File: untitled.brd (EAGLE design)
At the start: 54.8 x 54.7 mm, 25 parts

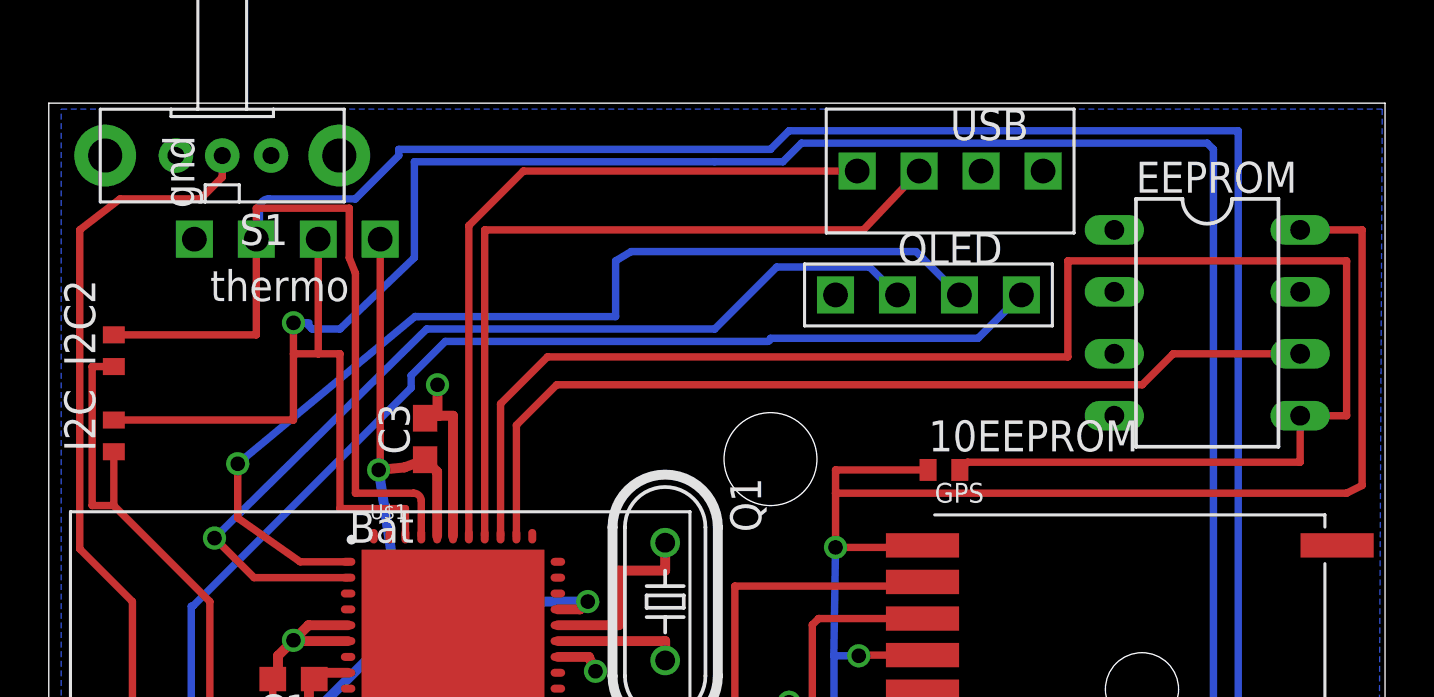
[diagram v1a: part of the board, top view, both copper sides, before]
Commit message: moved eeprom
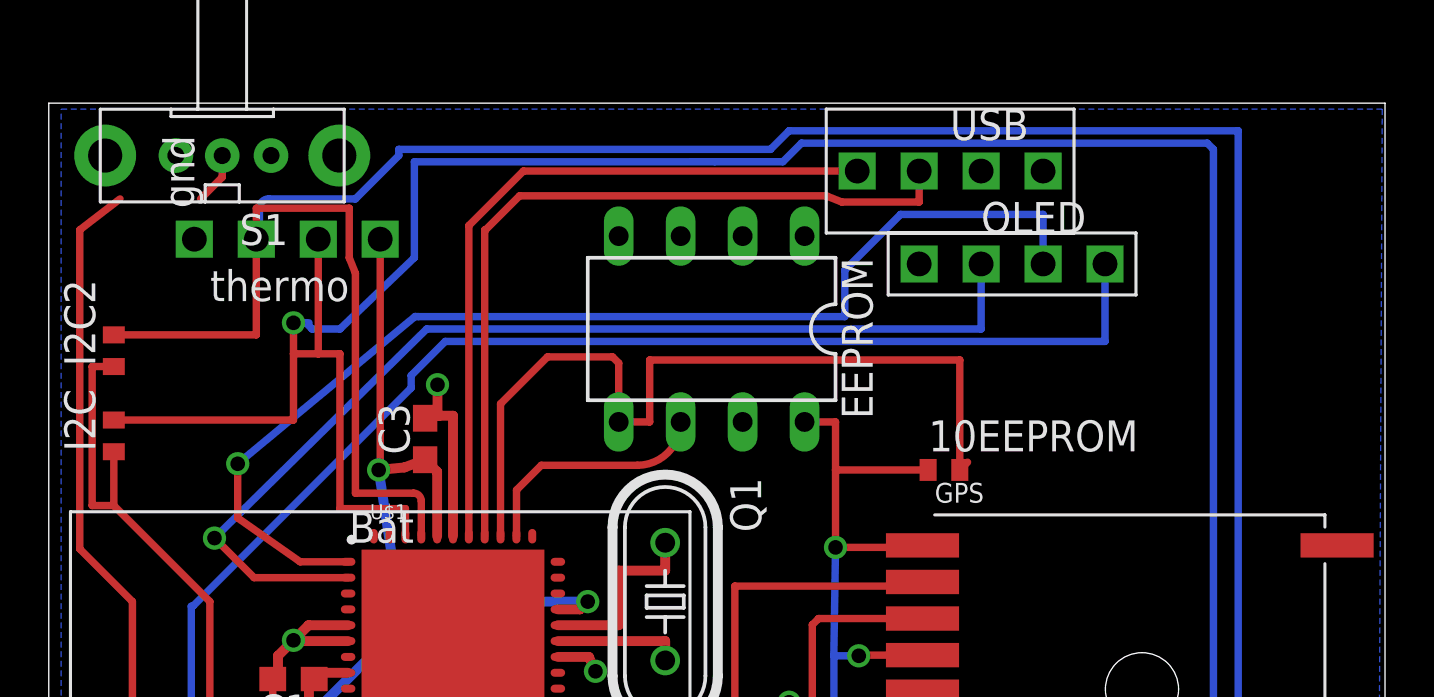
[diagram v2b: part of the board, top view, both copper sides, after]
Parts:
- moved EEPROM 20.3 mm to (65.4, 55.6), turned to 180 degrees
- moved OLED_SCREEN 3.66 mm to (79.0, 58.3)
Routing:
- net N$18: track 69.1 -> 35.1 mm
- net +3V3: track 270.3 -> 238.8 mm
- net N$19: track 37.9 -> 9.78 mm
- net +5V: track 57.5 -> 63.4 mm
- net N$11: track 42.2 -> 47.4 mm
- net N$10: track 39.2 -> 43.8 mm
- net N$13: track 28.9 -> 25.6 mm
- net N$9: track 31.4 -> 32.3 mm
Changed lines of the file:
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@@
 <wire x1="38.227" y1="64.887" x2="38.227" y2="10.16" width="0" layer="20"/>
 <text x="45.72" y="11.7475" size="1.778" layer="1">FG-1136</text>
-<hole x="67.818" y="50.292" drill="3.81"/>
 <rectangle x1="54.5465" y1="28.7655" x2="54.6735" y2="28.8925" layer="22"/>
 <rectangle x1="66.7385" y1="28.7655" x2="66.8655" y2="28.8925" layer="22"/>
@@
 <elements>
 <element name="5WAYSWITCH" library="5-wayswitch" package="5-WAYSWITCH" value="5-WAYSWITCH" x="64.77" y="16.51"/>
-<element name="EEPROM" library="adafruit" package="DIL08" value="DS1307" x="85.725" y="55.88" rot="R270"/>
+<element name="EEPROM" library="adafruit" package="DIL08" value="DS1307" x="65.405" y="55.626" rot="R180"/>
 <element name="GPS" library="adafruit" package="FGPMMOPA6B" value="" x="82.55" y="40.005"/>
 <element name="LIPOCHARGER-BOOSTER" library="SFLipoPack" package="SFLIPO" value="SFLIPO" x="46.736" y="36.703"/>
-<element name="OLED_SCREEN" library="4dScreen" package="4DSCREEN" value="4DSCREEN" x="75.565" y="57.023" rot="R270"/>
+<element name="OLED_SCREEN" library="4dScreen" package="4DSCREEN" value="4DSCREEN" x="78.994" y="58.293" rot="R270"/>
 <element name="RTC" library="adafruit" package="DIL08-ROUND" value="DS1302" x="64.77" y="28.575" rot="R270"/>
 <element name="S1" library="adafruit" package="EG1213" value="EG1213" x="45.339" y="62.738" rot="R180"/>
@@
 <contactref element="U$1" pad="37"/>
 <wire x1="56.1" y1="47.1313" x2="56.1" y2="59.69" width="0.3048" layer="1"/>
-<wire x1="56.1" y1="59.69" x2="71.628" y2="59.69" width="0.3048" layer="1"/>
-<wire x1="71.628" y1="59.69" x2="73.914" y2="62.103" width="0.3048" layer="1"/>
+<wire x1="73.914" y1="62.103" x2="73.914" y2="60.833" width="0.3048" layer="1"/>
+<wire x1="73.914" y1="60.833" x2="70.739" y2="60.833" width="0.3048" layer="1"/>
+<wire x1="70.739" y1="60.833" x2="70.104" y2="61.087" width="0.3048" layer="1"/>
+<wire x1="70.104" y1="61.087" x2="57.531" y2="61.087" width="0.3048" layer="1"/>
+<wire x1="57.531" y1="61.087" x2="56.134" y2="59.69" width="0.3048" layer="1"/>
+<wire x1="56.134" y1="59.69" x2="56.1" y2="59.69" width="0.3048" layer="1"/>
 </signal>
 <signal name="N$10">
@@
 <wire x1="46.6437" y1="45.4313" x2="45.0215" y2="47.0535" width="0.3048" layer="1"/>
 <wire x1="45.0215" y1="47.0535" x2="53.721" y2="55.626" width="0.3048" layer="16"/>
-<wire x1="53.721" y1="55.626" x2="65.532" y2="55.626" width="0.3048" layer="16"/>
-<wire x1="73.025" y1="57.023" x2="71.882" y2="58.166" width="0.3048" layer="16"/>
-<wire x1="71.882" y1="58.166" x2="68.072" y2="58.166" width="0.3048" layer="16"/>
-<wire x1="68.072" y1="58.166" x2="65.532" y2="55.626" width="0.3048" layer="16"/>
+<wire x1="53.721" y1="55.626" x2="76.454" y2="55.626" width="0.3048" layer="16"/>
+<wire x1="76.454" y1="58.293" x2="76.454" y2="55.626" width="0.3048" layer="16"/>
 </signal>
 <signal name="N$11">
@@
 <wire x1="48.5337" y1="46.0813" x2="45.974" y2="47.879" width="0.3048" layer="1"/>
 <wire x1="45.974" y1="47.879" x2="45.974" y2="50.1015" width="0.3048" layer="1"/>
-<wire x1="62.103" y1="58.801" x2="61.468" y2="58.42" width="0.3048" layer="16"/>
-<wire x1="61.468" y1="58.42" x2="61.468" y2="56.134" width="0.3048" layer="16"/>
-<wire x1="61.468" y1="56.134" x2="53.3793125" y2="56.134" width="0.3048" layer="16"/>
 <wire x1="53.3793125" y1="56.134" x2="53.24675" y2="56.1395625" width="0.3048" layer="16"/>
-<wire x1="75.565" y1="57.023" x2="73.787" y2="58.801" width="0.3048" layer="16"/>
-<wire x1="73.787" y1="58.801" x2="62.103" y2="58.801" width="0.3048" layer="16"/>
+<wire x1="53.3793125" y1="56.134" x2="70.866" y2="56.134" width="0.3048" layer="16"/>
+<wire x1="78.994" y1="58.293" x2="78.994" y2="60.325" width="0.3048" layer="16"/>
+<wire x1="78.994" y1="60.325" x2="73.152" y2="60.325" width="0.3048" layer="16"/>
+<wire x1="73.152" y1="60.325" x2="70.866" y2="58.039" width="0.3048" layer="16"/>
+<wire x1="70.866" y1="58.039" x2="70.866" y2="56.134" width="0.3048" layer="16"/>
 </signal>
 <signal name="N$18">
@@
 <contactref element="10EEPROM" pad="2"/>
 <wire x1="75.58" y1="49.8475" x2="75.8975" y2="50.165" width="0.3048" layer="1"/>
-<wire x1="75.8975" y1="50.165" x2="89.535" y2="50.165" width="0.3048" layer="1"/>
-<wire x1="89.535" y1="50.165" x2="89.535" y2="52.07" width="0.3048" layer="1"/>
 <wire x1="56.75" y1="47.1313" x2="56.75" y2="52.559" width="0.3048" layer="1"/>
-<wire x1="58.674" y1="54.483" x2="80.01" y2="54.483" width="0.3048" layer="1"/>
-<wire x1="80.01" y1="54.483" x2="80.01" y2="58.42" width="0.3048" layer="1"/>
-<wire x1="80.01" y1="58.42" x2="91.44" y2="58.42" width="0.3048" layer="1"/>
-<wire x1="91.44" y1="58.42" x2="91.44" y2="52.07" width="0.3048" layer="1"/>
-<wire x1="91.44" y1="52.07" x2="89.535" y2="52.07" width="0.3048" layer="1"/>
 <wire x1="58.674" y1="54.483" x2="56.75" y2="52.559" width="0.3048" layer="1"/>
+<wire x1="61.341" y1="54.483" x2="58.674" y2="54.483" width="0.3048" layer="1"/>
+<wire x1="61.341" y1="54.483" x2="61.595" y2="54.229" width="0.3048" layer="1"/>
+<wire x1="61.595" y1="54.229" x2="61.595" y2="51.816" width="0.3048" layer="1"/>
+<wire x1="61.595" y1="51.816" x2="62.865" y2="51.816" width="0.3048" layer="1"/>
+<wire x1="62.865" y1="51.816" x2="62.865" y2="54.356" width="0.3048" layer="1"/>
+<wire x1="62.865" y1="54.356" x2="75.58" y2="54.356" width="0.3048" layer="1"/>
+<wire x1="75.58" y1="54.356" x2="75.58" y2="49.8475" width="0.3048" layer="1"/>
 </signal>
 <signal name="N$19">
 <contactref element="U$1" pad="35"/>
 <contactref element="EEPROM" pad="6"/>
-<wire x1="57.4" y1="51.685" x2="57.4" y2="47.1313" width="0.3048" layer="1"/>
-<wire x1="84.328" y1="54.61" x2="83.058" y2="53.34" width="0.3048" layer="1"/>
-<wire x1="83.058" y1="53.34" x2="59.055" y2="53.34" width="0.3048" layer="1"/>
-<wire x1="57.4" y1="51.685" x2="59.055" y2="53.34" width="0.3048" layer="1"/>
-<wire x1="84.328" y1="54.61" x2="89.535" y2="54.61" width="0.3048" layer="1"/>
+<wire x1="57.4" y1="47.1313" x2="57.404" y2="47.1353" width="0.3048" layer="1"/>
+<wire x1="57.404" y1="47.1353" x2="57.404" y2="49.022" width="0.3048" layer="1"/>
+<wire x1="57.404" y1="49.022" x2="58.42" y2="50.038" width="0.3048" layer="1"/>
+<wire x1="58.42" y1="50.038" x2="62.357" y2="50.038" width="0.3048" layer="1"/>
+<wire x1="62.357" y1="50.038" x2="64.135" y2="51.816" width="0.3048" layer="1" curve="90"/>
 </signal>
 <signal name="N$13">
@@
 <wire x1="45.339" y1="62.738" x2="45.339" y2="61.849" width="0.3048" layer="1"/>
 <wire x1="45.339" y1="61.849" x2="44.45" y2="60.96" width="0.3048" layer="1"/>
-<wire x1="44.45" y1="60.96" x2="41.148" y2="60.96" width="0.3048" layer="1"/>
 <wire x1="39.497" y1="46.609" x2="39.497" y2="59.69" width="0.3048" layer="1"/>
 <wire x1="39.497" y1="59.69" x2="41.148" y2="60.96" width="0.3048" layer="1"/>
 <wire x1="39.497" y1="46.609" x2="41.656" y2="44.45" width="0.3048" layer="1"/>
 <wire x1="41.656" y1="44.45" x2="41.656" y2="39.243" width="0.3048" layer="1"/>
+<wire x1="41.148" y1="60.96" x2="44.45" y2="60.96" width="0" layer="19" extent="1-1"/>
 </signal>
 <signal name="N$14">
@@
 <contactref element="OLED_SCREEN" pad="5V"/>
 <contactref element="3.3LDO" pad="2"/>
-<wire x1="67.818" y1="55.245" x2="67.691" y2="55.118" width="0.3048" layer="16" curve="-90"/>
-<wire x1="67.691" y1="55.118" x2="54.483" y2="55.118" width="0.3048" layer="16"/>
+<wire x1="81.534" y1="55.118" x2="54.483" y2="55.118" width="0.3048" layer="16"/>
 <wire x1="44.069" y1="44.2595" x2="44.1325" y2="44.2595" width="0.3048" layer="16"/>
 <wire x1="44.1325" y1="44.2595" x2="53.086" y2="53.213" width="0.3048" layer="16"/>
@@
 <wire x1="44.069" y1="44.2595" x2="44.069" y2="34.163" width="0.3048" layer="16"/>
 <wire x1="44.069" y1="34.163" x2="41.656" y2="34.163" width="0.3048" layer="16"/>
-<wire x1="78.105" y1="57.023" x2="76.327" y2="55.245" width="0.3048" layer="16"/>
-<wire x1="76.327" y1="55.245" x2="67.818" y2="55.245" width="0.3048" layer="16"/>
+<wire x1="81.534" y1="58.293" x2="81.534" y2="55.118" width="0.3048" layer="16"/>
 </signal>
 <signal name="+3V3">
@@
 <wire x1="73.9675" y1="46.6725" x2="70.485" y2="46.6725" width="0.3048" layer="1"/>
 <wire x1="74.28" y1="49.8475" x2="70.485" y2="49.8475" width="0.3048" layer="1"/>
-<wire x1="70.485" y1="49.8475" x2="70.485" y2="48.895" width="0.3048" layer="1"/>
-<wire x1="70.485" y1="48.895" x2="70.485" y2="46.6725" width="0.3048" layer="1"/>
-<wire x1="89.535" y1="59.69" x2="92.075" y2="59.69" width="0.3048" layer="1"/>
-<wire x1="92.075" y1="59.69" x2="92.075" y2="49.2125" width="0.3048" layer="1"/>
-<wire x1="92.075" y1="49.2125" x2="91.44" y2="48.895" width="0.3048" layer="1"/>
-<wire x1="91.44" y1="48.895" x2="70.485" y2="48.895" width="0.3048" layer="1"/>
+<wire x1="70.485" y1="49.8475" x2="70.485" y2="46.6725" width="0.3048" layer="1"/>
 <wire x1="91.395" y1="21.895" x2="84.595" y2="21.895" width="0.3048" layer="1"/>
 <wire x1="84.595" y1="21.895" x2="84.595" y2="19.095" width="0.3048" layer="1"/>
@@
 <wire x1="40.005" y1="54.087" x2="40.005" y2="48.387" width="0.3048" layer="1"/>
 <wire x1="40.005" y1="48.387" x2="40.894" y2="48.387" width="0.3048" layer="1"/>
+<wire x1="69.215" y1="51.816" x2="70.485" y2="51.816" width="0.3048" layer="1"/>
+<wire x1="70.485" y1="51.816" x2="70.485" y2="49.8475" width="0.3048" layer="1"/>
 </signal>
 </signals>
